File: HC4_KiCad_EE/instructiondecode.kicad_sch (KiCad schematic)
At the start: 26 parts, among them IC11 74HC74, IC12 74HC00, IC13 74HC4053, IC14 74HC02

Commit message: たぶん完成！！！！！！！
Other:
- title: HC4_CPU -> HC4e_CPU
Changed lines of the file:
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@@
 	(paper "A4")
 	(title_block
-		(title "HC4_CPU")
-		(date "2025-06-16")
+		(title "HC4e_CPU")
+		(date "2025-07-21")
 		(rev "1.0")
 	)

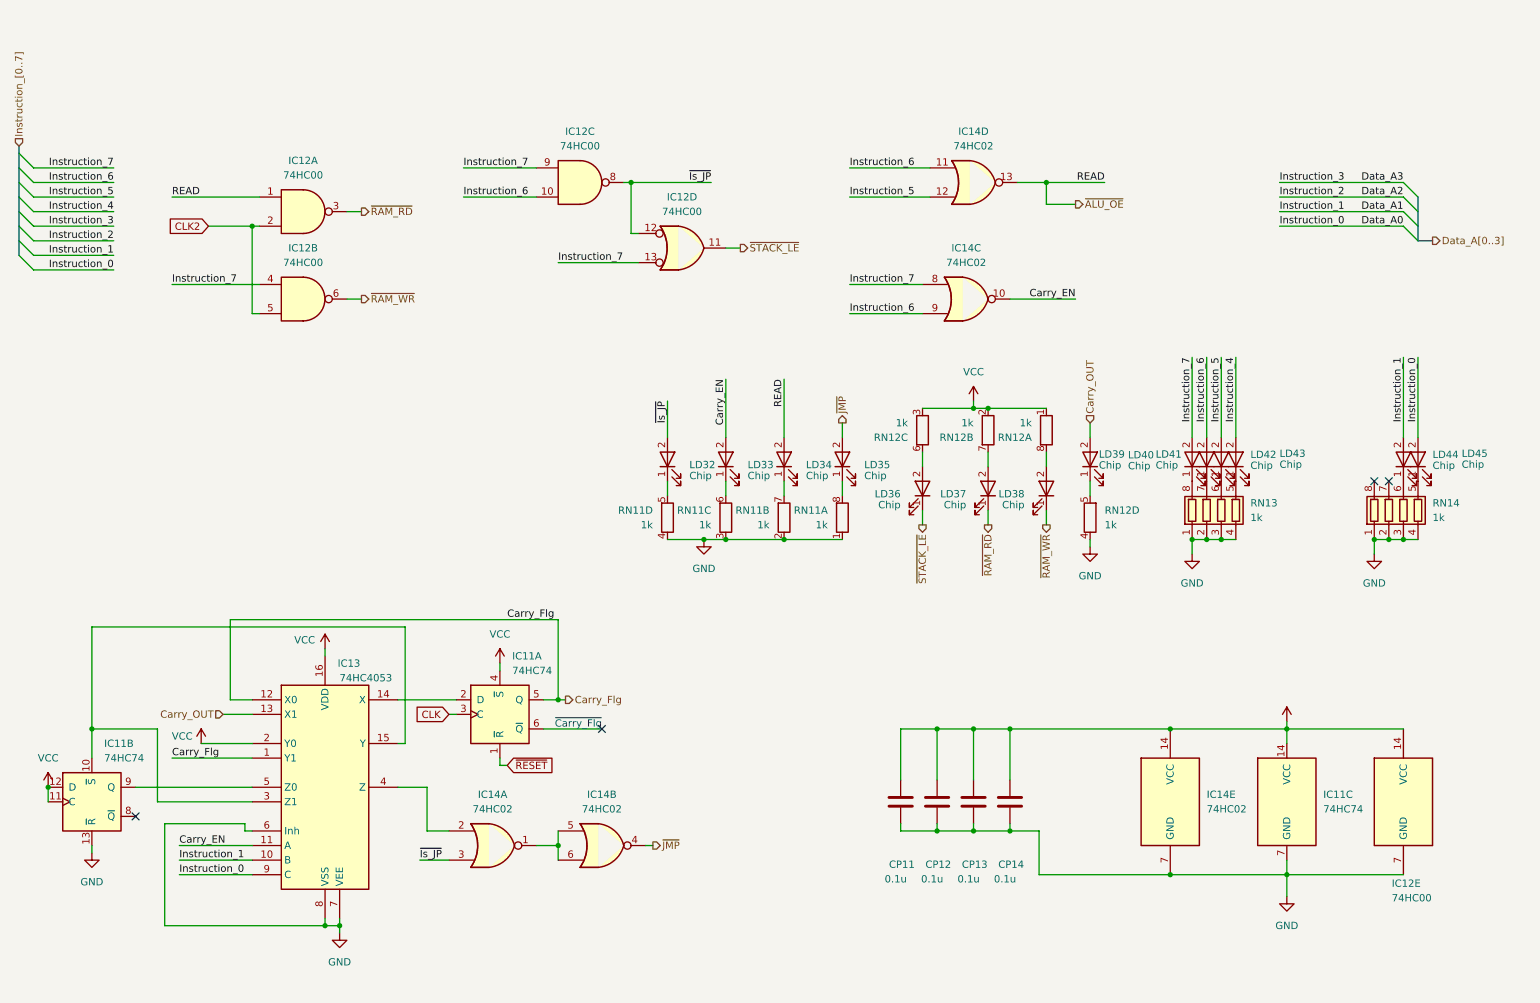
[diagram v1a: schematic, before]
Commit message: 妥協に妥協を重ね妥協を加速する あとクロックの起動が安定しないのを直した
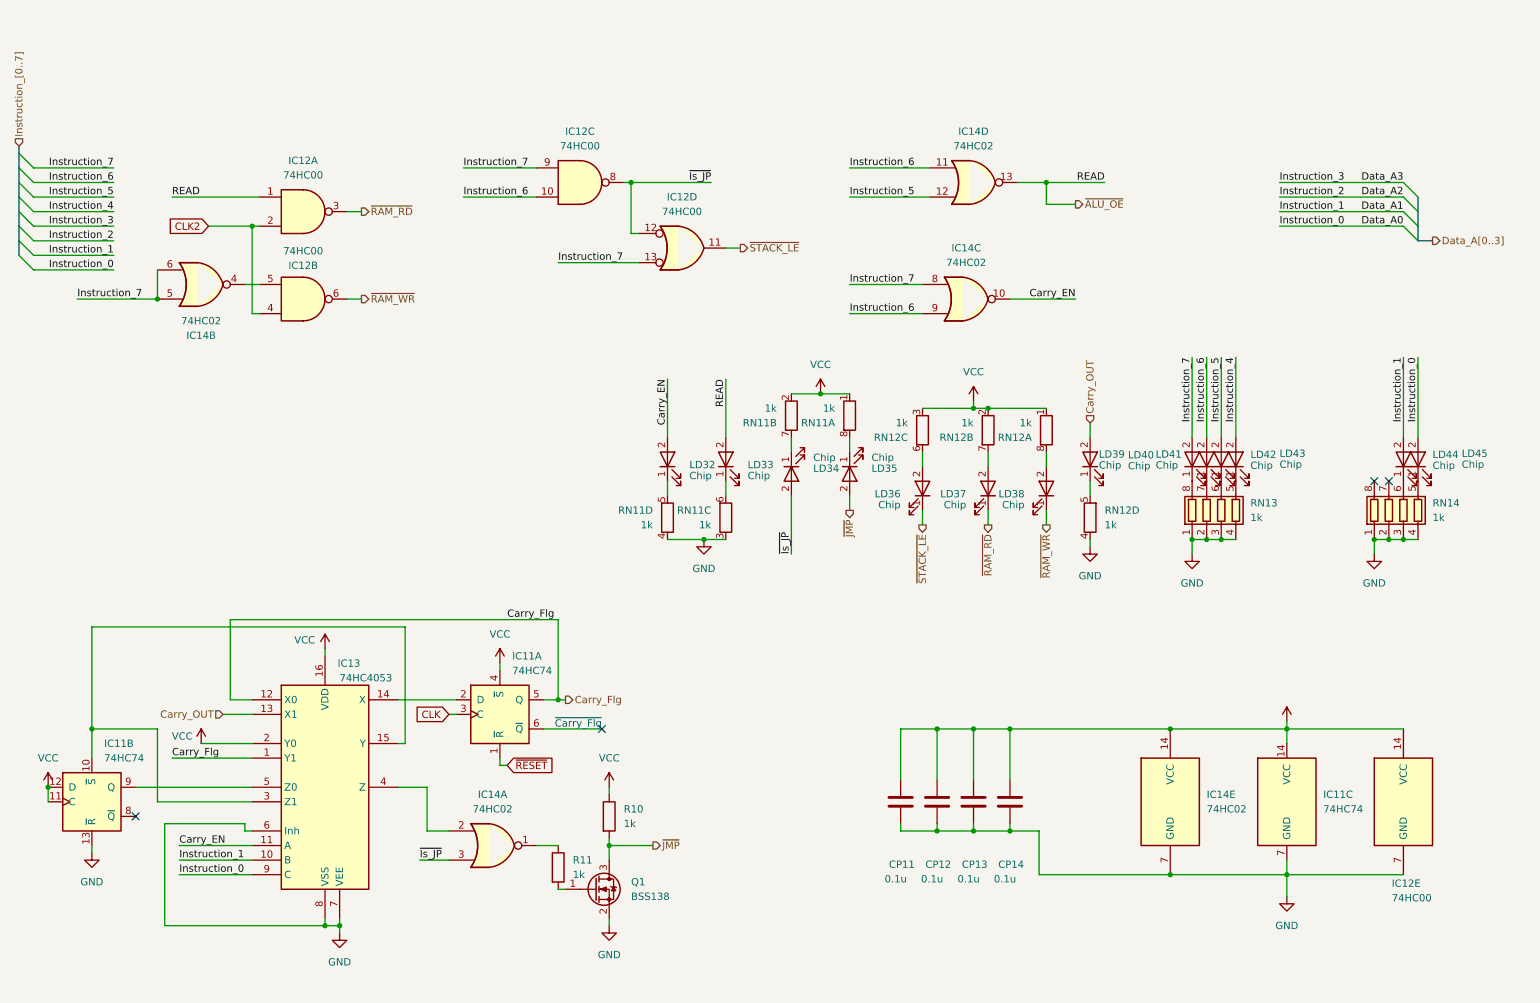
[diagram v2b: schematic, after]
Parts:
- added Q1: BSS138, Package_TO_SOT_SMD:SOT-23, symbol Transistor_FET:BSS138
- added R10, R11: 1k, Resistor_SMD:R_0603_1608Metric, symbol Device:R
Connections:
- net CLK2: now also IC12.4; no longer IC12.5
- net Carry_EN: now also LD32.2; no longer LD33.2
- net GND: now also Q1.2 (S); no longer RN11.1 (R1.1), RN11.2 (R2.1)
- net Instruction_7: now also IC14.5, IC14.6; no longer IC12.4
- net VCC: now also RN11.1 (R1.1), RN11.2 (R2.1), R10.1
- net ~{ALU_OE}: now also LD33.2; no longer LD34.2
- net ~{Is_JP}: now also LD34.2; no longer LD32.2
- net ~{JMP}: now also Q1.3 (D), R10.2; no longer IC14.4
- new net: Q1.1 (G), R11.2
- new net: IC12.5, IC14.4
- new net: IC14.1, R11.1
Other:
- moved on the sheet: LD34, LD35, RN11A, RN11B

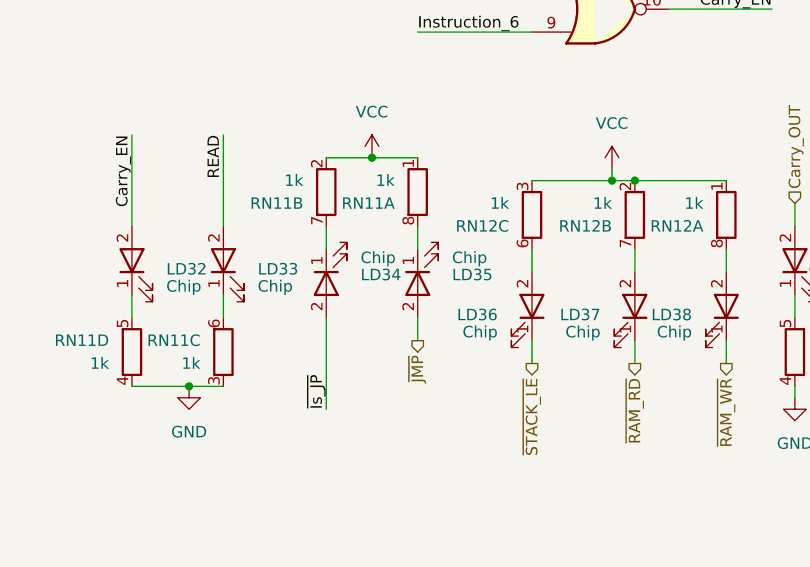
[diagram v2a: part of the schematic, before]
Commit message: Update KiCad project files and schematic components
- Changed active layer from 0 to 5 in HC4_KiCad_EE.kicad_prl.
- Adjusted minimum resolved spokes from 2 to 1 and updated solder mask clearance in HC4_KiCad_EE.kicad_pro.
- Corrected resistor value from "3.9k" to "390" in clockandreset.kicad_sch.
- Added fabrication toolkit options JSON file for project configuration.
- Modified LED component positions in instructiondecode.kicad_sch for better alignment.
- Created .gitignore file in production directory to exclude unnecessary files.
- Added HC4e_Rev01.zip to production directory for project release.
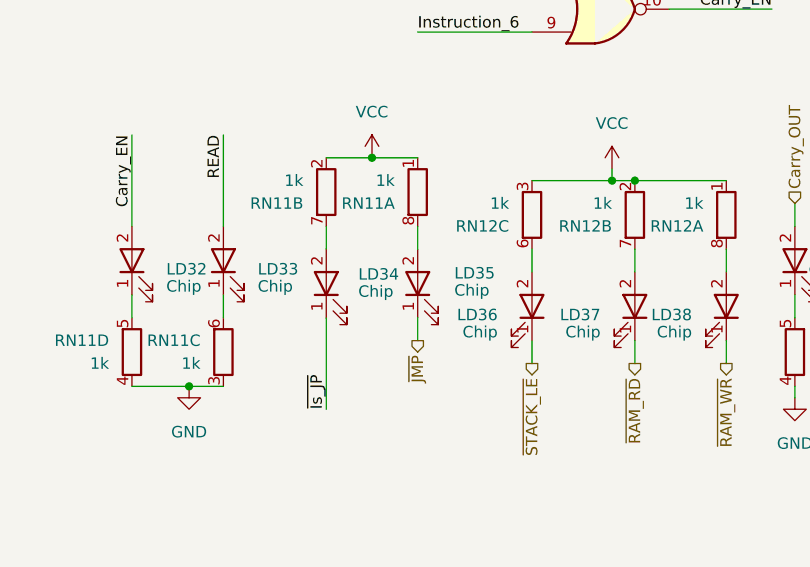
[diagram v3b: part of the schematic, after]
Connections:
- net ~{Is_JP}: now also LD34.1 (K); no longer LD34.2
- net ~{JMP}: now also LD35.1 (K); no longer LD35.2
- net at RN11.8 (R1.2): now also LD35.2; no longer LD35.1 (K)
- net at RN11.7 (R2.2): now also LD34.2; no longer LD34.1 (K)
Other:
- moved on the sheet: LD34, LD35
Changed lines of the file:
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@@
 		(lib_id "Device2:LED_")
 		(at 165.1 91.44 90)
-		(mirror x)
 		(unit 1)
 		(exclude_from_sim no)
@@
 		(on_board yes)
 		(dnp no)
-		(fields_autoplaced yes)
 		(property "Reference" "LD35"
-			(at 168.91 90.4876 90)
+			(at 169.164 90.2969 90)
 			(effects
 				(font
@@
 		)
 		(property "Value" "Chip"
-			(at 168.91 88.5825 90)
+			(at 169.164 92.202 90)
 			(effects
 				(font
@@
 		(lib_id "Device2:LED_")
 		(at 154.94 91.44 90)
-		(mirror x)
 		(unit 1)
 		(exclude_from_sim no)
@@
 		(on_board yes)
 		(dnp no)
-		(fields_autoplaced yes)
 		(property "Reference" "LD34"
-			(at 158.75 90.4876 90)
+			(at 158.496 90.424 90)
 			(effects
 				(font
@@
 		)
 		(property "Value" "Chip"
-			(at 158.75 88.5825 90)
-			(effects
-				(font
+			(at 158.496 92.3291 90)
+			(effects
+				(font

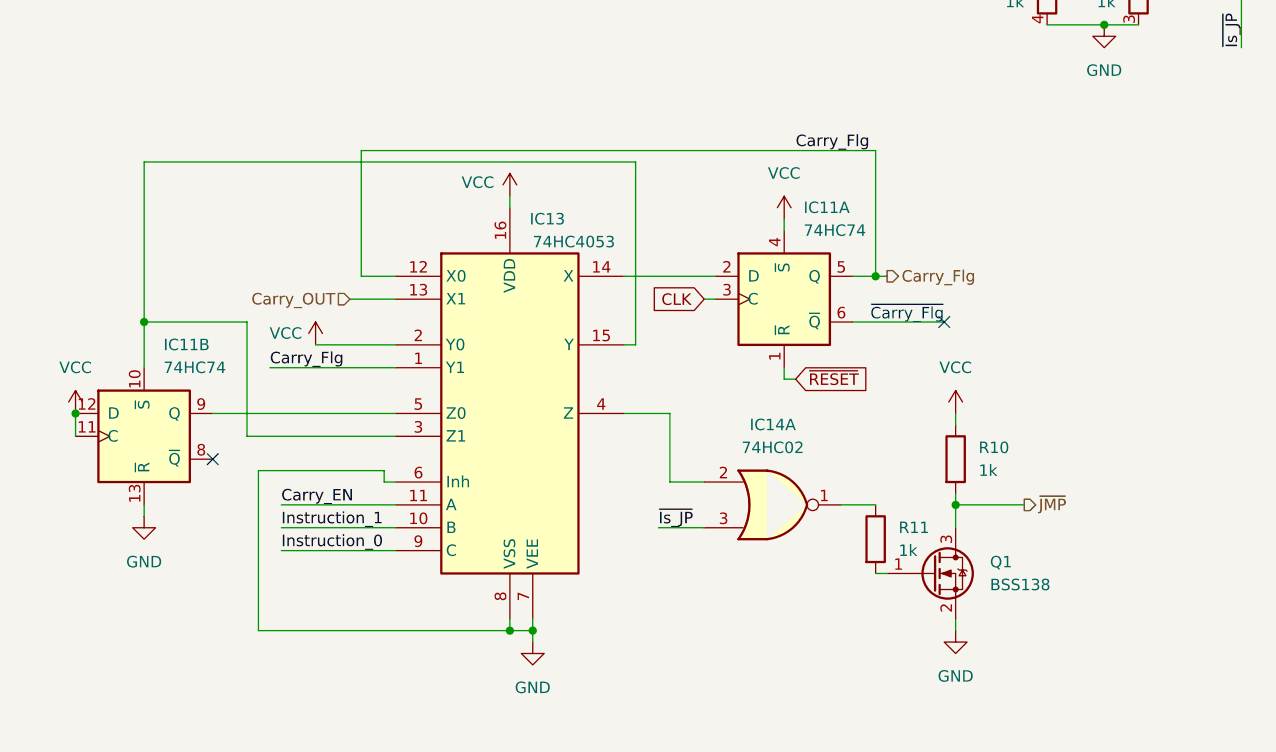
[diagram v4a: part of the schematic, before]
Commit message: MOSFETを回路上より排除
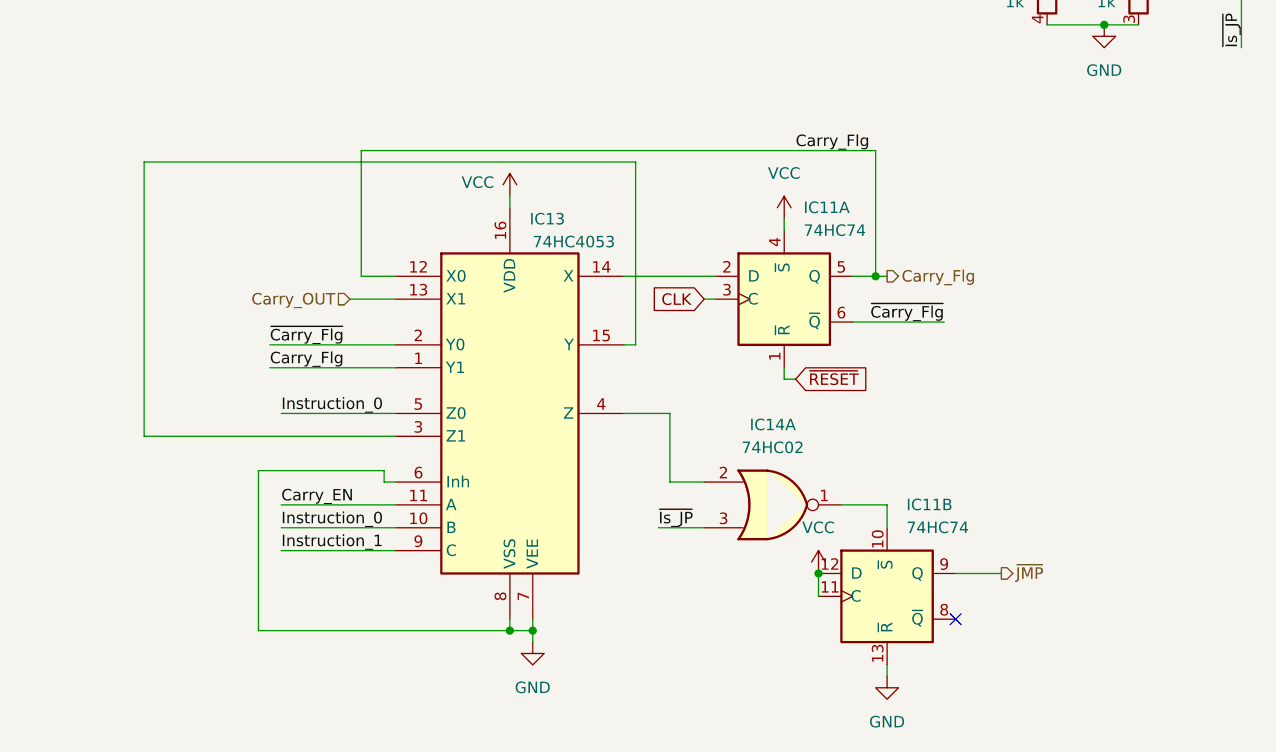
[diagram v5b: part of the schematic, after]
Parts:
- removed Q1: BSS138, Package_TO_SOT_SMD:SOT-23, symbol Transistor_FET:BSS138
- removed R10, R11: 1k, Resistor_SMD:R_0603_1608Metric, symbol Device:R
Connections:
- net Data_A0: now also IC13.10 (B), IC13.5 (Z0); no longer IC13.9 (C)
- net Data_A1: now also IC13.9 (C); no longer IC13.10 (B)
- net VCC: no longer IC13.2 (Y0)
- net ~{JMP}: now also IC11.9 (Q)
- net at IC13.15 (Y), IC13.3 (Z1): no longer IC11.10 (~{S})
- net ~{Carry_Flg}: now reaches IC11.6 (~{Q})
- net ~{Carry_Flg}: now also IC13.2 (Y0)
- net at IC14.1: now also IC11.10 (~{S})
- no-connect marks 4 -> 3
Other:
- note removed: "~{Carry_Flg}"

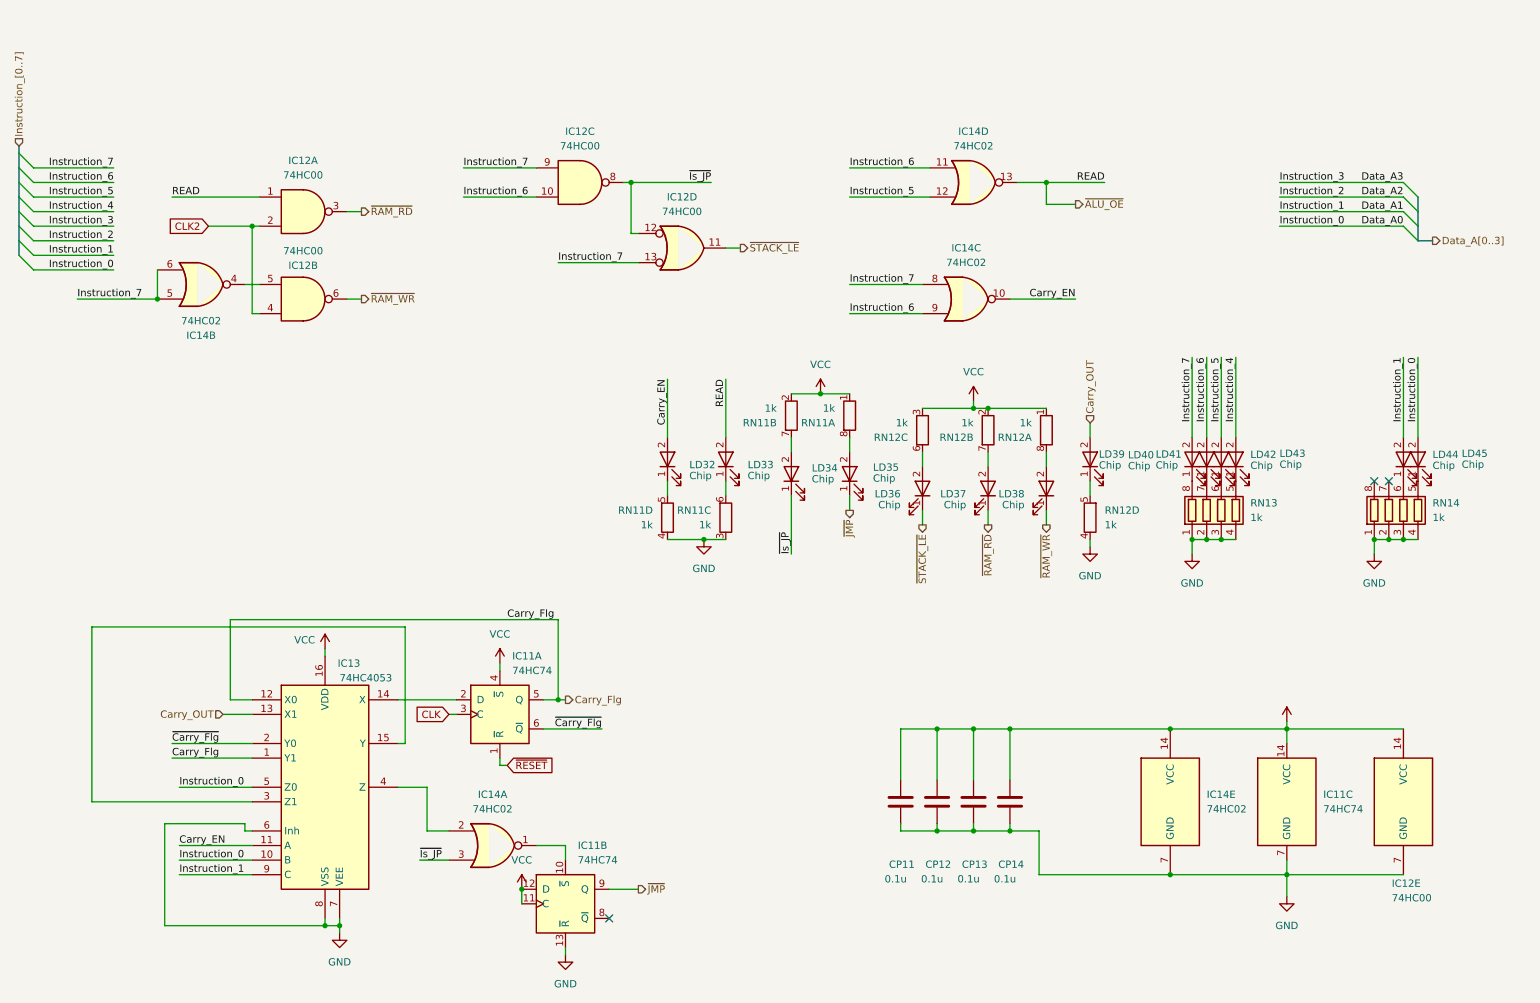
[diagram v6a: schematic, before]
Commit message: feat:HC4e改版,BOMを令和最新版に更新,KiCadを10に更新
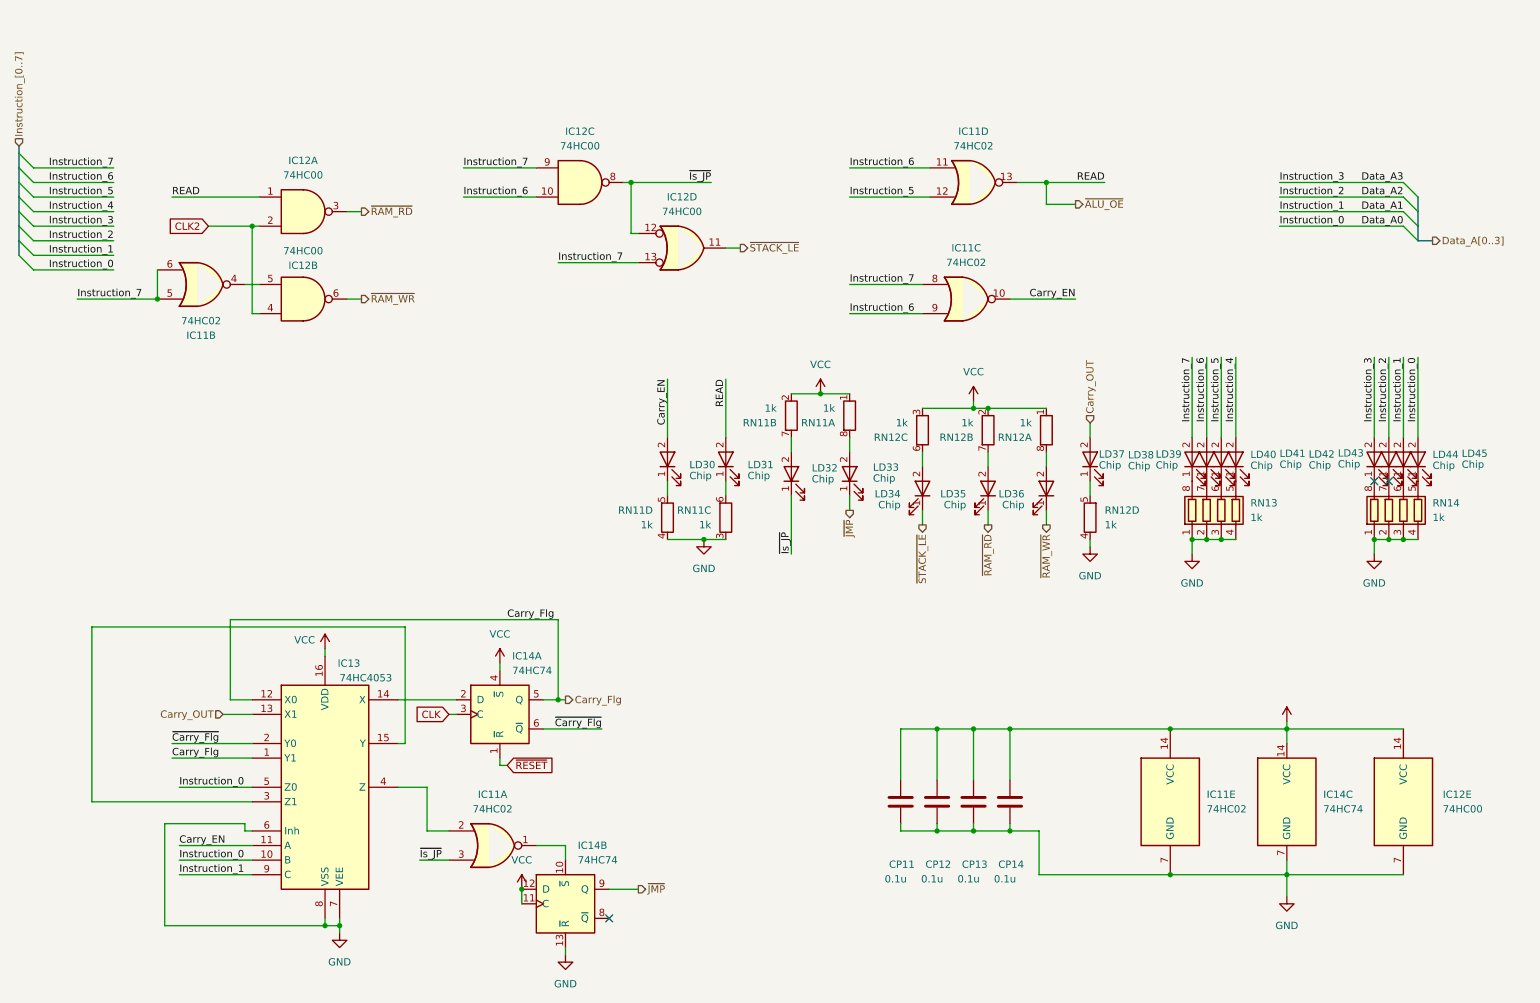
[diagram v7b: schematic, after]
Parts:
- added LD42, LD43: Chip, LED_SMD:LED_0603_1608Metric, symbol Device2:LED_
- IC11: renamed from IC14; footprint Package_SO:SO-14_5.3x10.2mm_P1.27mm -> (none)
- IC12: footprint Package_SO:SO-14_5.3x10.2mm_P1.27mm -> (none)
- renumbered IC11 to IC14, LD32 to LD30, LD33 to LD31, LD34 to LD32, LD35 to LD33, LD36 to LD34, LD37 to LD35, LD38 to LD36, LD39 to LD37, LD40 to LD38, LD41 to LD39, LD42 to LD40, LD43 to LD41
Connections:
- net Data_A2: now also LD43.2
- net Data_A3: now also LD42.2
- net at RN14.7 (R2.2): now also LD43.1 (K)
- net at RN14.8 (R1.2): now also LD42.1 (K)
